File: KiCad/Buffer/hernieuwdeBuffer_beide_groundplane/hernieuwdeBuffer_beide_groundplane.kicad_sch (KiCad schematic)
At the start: 44 parts, among them J1 Conn_01x04_Female, J2 DCJ200-10-A-XX-X_REVA, J3 Rood, J4 Groen, J5 Oranje1, J6 Oranje2, SW1 ENABLE, SW2 BOOT, T1 signaal oranje, T10 o3r, T11 o4r, T12 o5r, T13 06r, T14 r1, T15 r2, T16 r3, T17 r4, T18 r5, T19 g1, T2 o1g, T20 g2, T21 g3, T22 g4, T23 g5, T3 o2g, T4 o3g, T5 o4g, T6 o5g, T7 06g, T8 o1r, T9 o2r, U1 ESP32-WROOM-32E_(16MB), U2 AMS1117

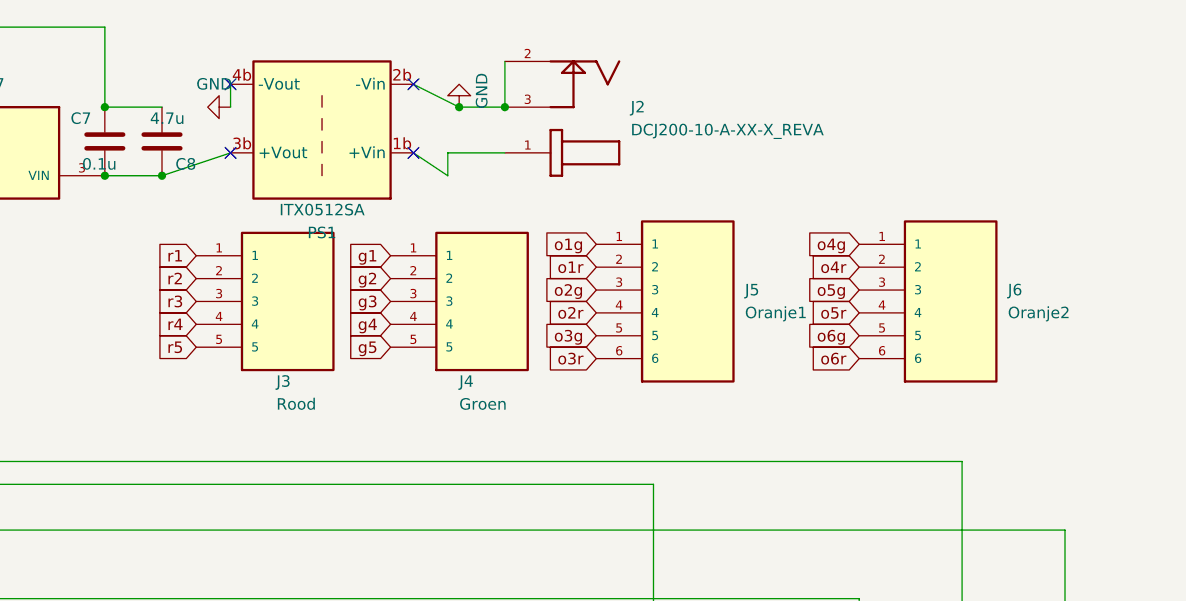
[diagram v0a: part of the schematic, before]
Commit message: updates kroonsteentjes naar 2.54mm voor 7segment en buffer
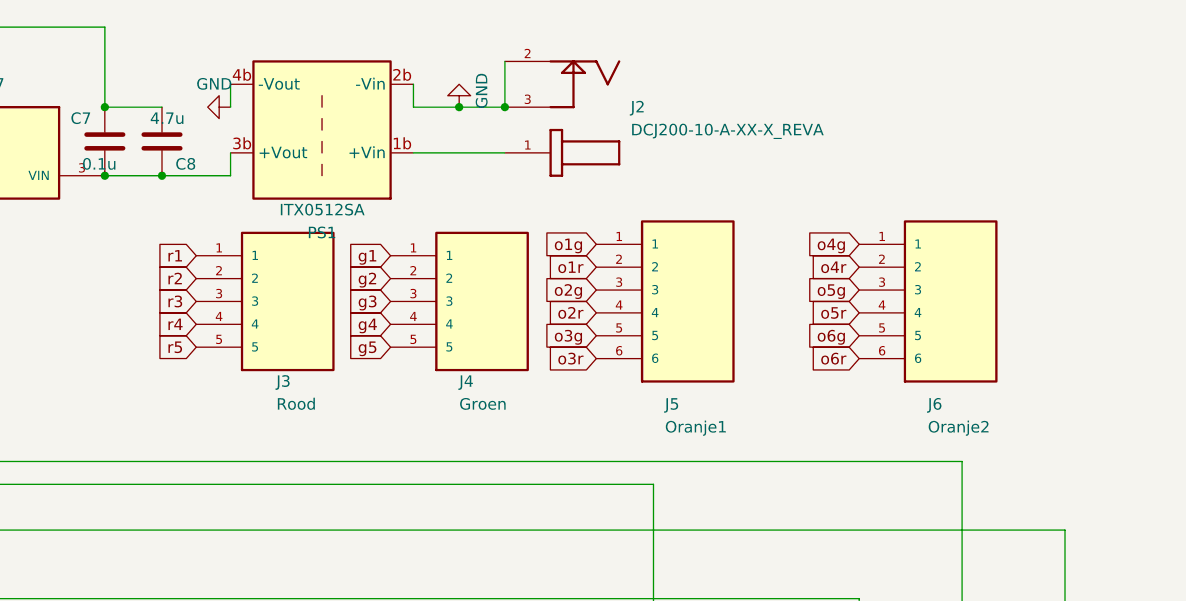
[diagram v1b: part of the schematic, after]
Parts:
- J3, J4: footprint libraries:TE_282841-5 -> (none)
- J5, J6: footprint libraries:TE_282841-6 -> (none)
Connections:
- no-connect marks 10 -> 6
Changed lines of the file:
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@@
   (junction (at 113.03 31.75) (diameter 0) (color 0 0 0 0)
   )
+  (junction (at 205.74 24.13) (diameter 0) (color 0 0 0 0)
+  )
+  (junction (at 172.72 31.75) (diameter 0) (color 0 0 0 0)
+  )
   (junction (at 101.6 142.24) (diameter 0) (color 0 0 0 0)
   )
-  (junction (at 205.74 24.13) (diameter 0) (color 0 0 0 0)
-  )
   (junction (at 144.78 15.24) (diameter 0) (color 0 0 0 0)
   )
   (junction (at 127 172.72) (diameter 0) (color 0 0 0 0)
-  )
-  (junction (at 172.72 31.75) (diameter 0) (color 0 0 0 0)
   )
   (junction (at 101.6 129.54) (diameter 0) (color 0 0 0 0)
@@
   (no_connect (at 87.63 76.2))
   (no_connect (at 46.99 66.04))
-  (no_connect (at 180.34 29.21))
   (no_connect (at 46.99 68.58))
-  (no_connect (at 200.66 29.21))
-  (no_connect (at 200.66 21.59))
   (no_connect (at 46.99 78.74))
   (no_connect (at 46.99 76.2))
-  (no_connect (at 180.34 21.59))
   (wire (pts (xy 180.34 21.59) (xy 180.34 24.13))
     (stroke (width 0) (type default) (color 0 0 0 0))
@@
     (stroke (width 0) (type default) (color 0 0 0 0))
   )
-  (wire (pts (xy 204.47 29.21) (xy 204.47 31.75))
-    (stroke (width 0) (type default) (color 0 0 0 0))
-  )
   (wire (pts (xy 121.92 138.43) (xy 121.92 142.24))
     (stroke (width 0) (type default) (color 0 0 0 0))
@@
     (stroke (width 0) (type default) (color 0 0 0 0))
   )
+  (wire (pts (xy 180.34 31.75) (xy 172.72 31.75))
+    (stroke (width 0) (type default) (color 0 0 0 0))
+  )
   (wire (pts (xy 87.63 93.98) (xy 161.29 93.98))
     (stroke (width 0) (type default) (color 0 0 0 0))
@@
     (stroke (width 0) (type default) (color 0 0 0 0))
   )
-  (wire (pts (xy 200.66 29.21) (xy 204.47 31.75))
-    (stroke (width 0) (type default) (color 0 0 0 0))
-  )
   (wire (pts (xy 102.87 31.75) (xy 113.03 31.75))
     (stroke (width 0) (type default) (color 0 0 0 0))
@@
     (stroke (width 0) (type default) (color 0 0 0 0))
   )
+  (wire (pts (xy 200.66 29.21) (xy 210.82 29.21))
+    (stroke (width 0) (type default) (color 0 0 0 0))
+  )
   (wire (pts (xy 250.19 78.74) (xy 87.63 78.74))
     (stroke (width 0) (type default) (color 0 0 0 0))
@@
     (stroke (width 0) (type default) (color 0 0 0 0))
   )
+  (wire (pts (xy 205.74 24.13) (xy 200.66 24.13))
+    (stroke (width 0) (type default) (color 0 0 0 0))
+  )
   (polyline (pts (xy 284.48 109.22) (xy 284.48 152.4))
     (stroke (width 0) (type default) (color 0 0 0 0))
@@
     (stroke (width 0) (type default) (color 0 0 0 0))
   )
+  (wire (pts (xy 200.66 24.13) (xy 200.66 21.59))
+    (stroke (width 0) (type default) (color 0 0 0 0))
+  )
   (wire (pts (xy 132.08 15.24) (xy 132.08 24.13))
     (stroke (width 0) (type default) (color 0 0 0 0))
@@
     (stroke (width 0) (type default) (color 0 0 0 0))
   )
-  (wire (pts (xy 180.34 29.21) (xy 172.72 31.75))
+  (wire (pts (xy 180.34 29.21) (xy 180.34 31.75))
     (stroke (width 0) (type default) (color 0 0 0 0))
   )
@@
     (stroke (width 0) (type default) (color 0 0 0 0))
   )
-  (wire (pts (xy 204.47 29.21) (xy 210.82 29.21))
-    (stroke (width 0) (type default) (color 0 0 0 0))
-  )
   (wire (pts (xy 127 134.62) (xy 142.24 134.62))
     (stroke (width 0) (type default) (color 0 0 0 0))
   )
   (polyline (pts (xy 88.9 190.5) (xy 152.4 190.5))
-    (stroke (width 0) (type default) (color 0 0 0 0))
-  )
-  (wire (pts (xy 200.66 21.59) (xy 205.74 24.13))
     (stroke (width 0) (type default) (color 0 0 0 0))
   )
@@
   )
   (symbol (lib_id "282841-6:282841-6") (at 260.35 46.99 0) (unit 1)
-    (in_bom yes) (on_board yes) (fields_autoplaced)
-    (property "Reference" "J6" (id 0) (at 266.7 44.4499 0)
-      (effects (font (size 1.27 1.27)) (justify left))
-    )
-    (property "Value" "Oranje2" (id 1) (at 266.7 46.9899 0)
-      (effects (font (size 1.27 1.27)) (justify left))
-    )
-    (property "Footprint" "libraries:TE_282841-6" (id 2) (at 260.35 46.99 0)
+    (in_bom yes) (on_board yes)
+    (property "Reference" "J6" (id 0) (at 257.81 57.15 0)
+      (effects (font (size 1.27 1.27)) (justify left))
+    )
+    (property "Value" "Oranje2" (id 1) (at 257.81 59.69 0)
+      (effects (font (size 1.27 1.27)) (justify left))
+    )
+    (property "Footprint" "" (id 2) (at 260.35 46.99 0)
       (effects (font (size 1.27 1.27)) (justify left bottom) hide)
     )
@@
       (effects (font (size 1.27 1.27)) (justify left))
     )
-    (property "Footprint" "libraries:TE_282841-5" (id 2) (at 186.69 45.72 0)
+    (property "Footprint" "" (id 2) (at 186.69 45.72 0)
       (effects (font (size 1.27 1.27)) (justify left bottom) hide)
     )
@@
   )
   (symbol (lib_id "282841-6:282841-6") (at 231.14 46.99 0) (unit 1)
-    (in_bom yes) (on_board yes) (fields_autoplaced)
-    (property "Reference" "J5" (id 0) (at 237.49 44.4499 0)
-      (effects (font (size 1.27 1.27)) (justify left))
-    )
-    (property "Value" "Oranje1" (id 1) (at 237.49 46.9899 0)
-      (effects (font (size 1.27 1.27)) (justify left))
-    )
-    (property "Footprint" "libraries:TE_282841-6" (id 2) (at 231.14 46.99 0)
+    (in_bom yes) (on_board yes)
+    (property "Reference" "J5" (id 0) (at 228.6 57.15 0)
+      (effects (font (size 1.27 1.27)) (justify left))
+    )
+    (property "Value" "Oranje1" (id 1) (at 228.6 59.69 0)
+      (effects (font (size 1.27 1.27)) (justify left))
+    )
+    (property "Footprint" "" (id 2) (at 231.14 46.99 0)
       (effects (font (size 1.27 1.27)) (justify left bottom) hide)
     )
@@
       (effects (font (size 1.27 1.27)) (justify left))
     )
-    (property "Footprint" "libraries:TE_282841-5" (id 2) (at 208.28 45.72 0)
+    (property "Footprint" "" (id 2) (at 208.28 45.72 0)
       (effects (font (size 1.27 1.27)) (justify left bottom) hide)
     )
@@
     )
     (path "/393d76fe-fb48-41a1-a304-c52186da1c75"
-      (reference "J3") (unit 1) (value "Rood") (footprint "libraries:TE_282841-5")
+      (reference "J3") (unit 1) (value "Rood") (footprint "libraries:TE_1546215-5")
     )
     (path "/61bf3265-f25c-4b8e-bad1-265f76b676cb"
-      (reference "J4") (unit 1) (value "Groen") (footprint "libraries:TE_282841-5")
+      (reference "J4") (unit 1) (value "Groen") (footprint "libraries:TE_1546215-5")
     )
     (path "/5506dcd3-dfaf-4f6a-b8ea-1bc1762966d2"
-      (reference "J5") (unit 1) (value "Oranje1") (footprint "libraries:TE_282841-6")
+      (reference "J5") (unit 1) (value "Oranje1") (footprint "libraries:TE_1546215-6")
     )
     (path "/2fa9a3e8-428b-41d7-9cee-a7468b8be148"
-      (reference "J6") (unit 1) (value "Oranje2") (footprint "libraries:TE_282841-6")
+      (reference "J6") (unit 1) (value "Oranje2") (footprint "libraries:TE_1546215-6")
     )
     (path "/a7b84331-134a-455a-997c-cfa297a6b47d"

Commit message: fiets hermaakt (2 versies level shifter)
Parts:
- J3, J4: footprint (none) -> libraries:TE_1546215-5
- J5, J6: footprint (none) -> libraries:TE_1546215-6
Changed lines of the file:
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@@
       (effects (font (size 1.27 1.27)) (justify left))
     )
-    (property "Footprint" "" (id 2) (at 260.35 46.99 0)
+    (property "Footprint" "libraries:TE_1546215-6" (id 2) (at 260.35 46.99 0)
       (effects (font (size 1.27 1.27)) (justify left bottom) hide)
     )
@@
       (effects (font (size 1.27 1.27)) (justify left))
     )
-    (property "Footprint" "" (id 2) (at 186.69 45.72 0)
+    (property "Footprint" "libraries:TE_1546215-5" (id 2) (at 186.69 45.72 0)
       (effects (font (size 1.27 1.27)) (justify left bottom) hide)
     )
@@
       (effects (font (size 1.27 1.27)) (justify left))
     )
-    (property "Footprint" "" (id 2) (at 231.14 46.99 0)
+    (property "Footprint" "libraries:TE_1546215-6" (id 2) (at 231.14 46.99 0)
       (effects (font (size 1.27 1.27)) (justify left bottom) hide)
     )
@@
       (effects (font (size 1.27 1.27)) (justify left))
     )
-    (property "Footprint" "" (id 2) (at 208.28 45.72 0)
-      (effects (font (size 1.27 1.27)) (justify left bottom) hide)
-    )
+    (property "Footprint" "libraries:TE_1546215-5" (id 2) (at 208.28 45.72 0)
+      (effects (font (size 1.27 1.27)) (justify left bottom) hide)
+    )
